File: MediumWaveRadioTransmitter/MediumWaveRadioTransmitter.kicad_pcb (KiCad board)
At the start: 2 copper layers, 16 parts, among them J1 Screw_Terminal_01x05, P6 100R, T3 BC337, T4 BC337, Y1 400 kH

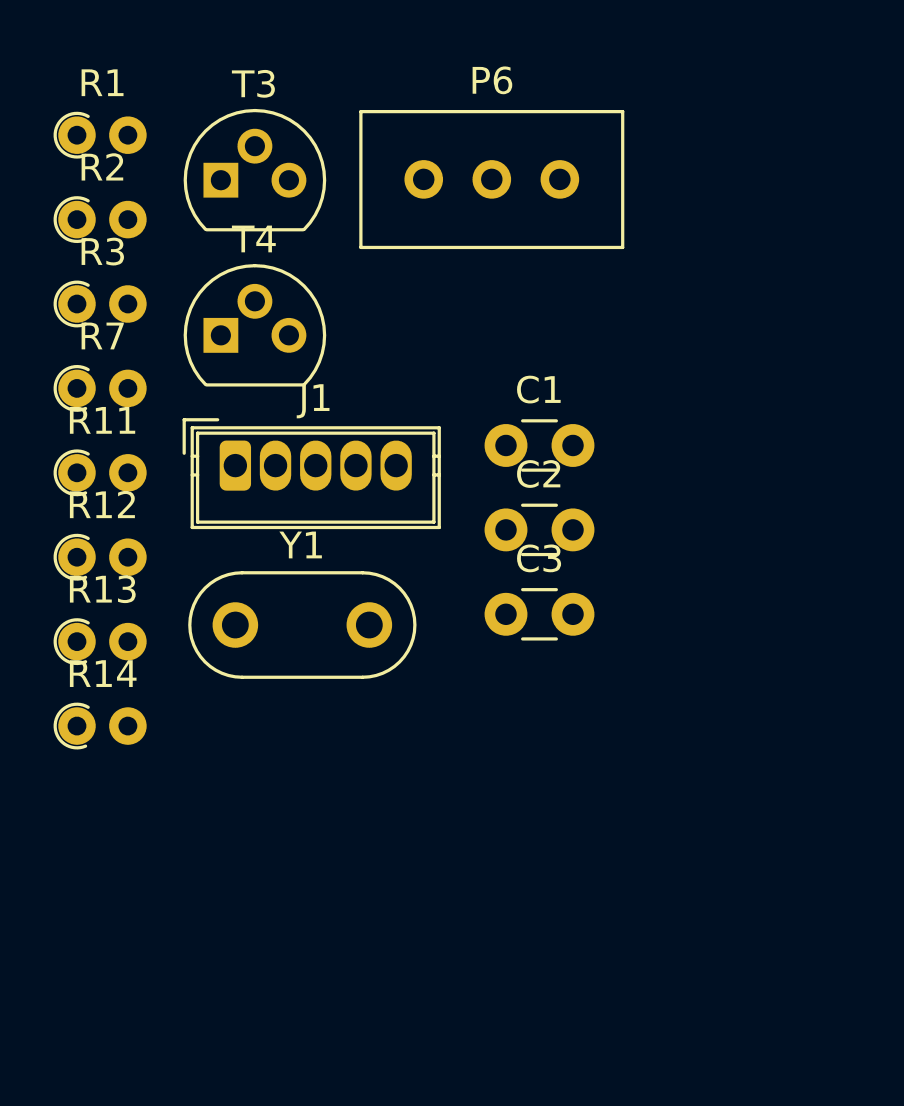
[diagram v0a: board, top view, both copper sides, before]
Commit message: feat: circuit diagram improved
changes:
- circuit diagram improved
- pcb layout routed

closes #1
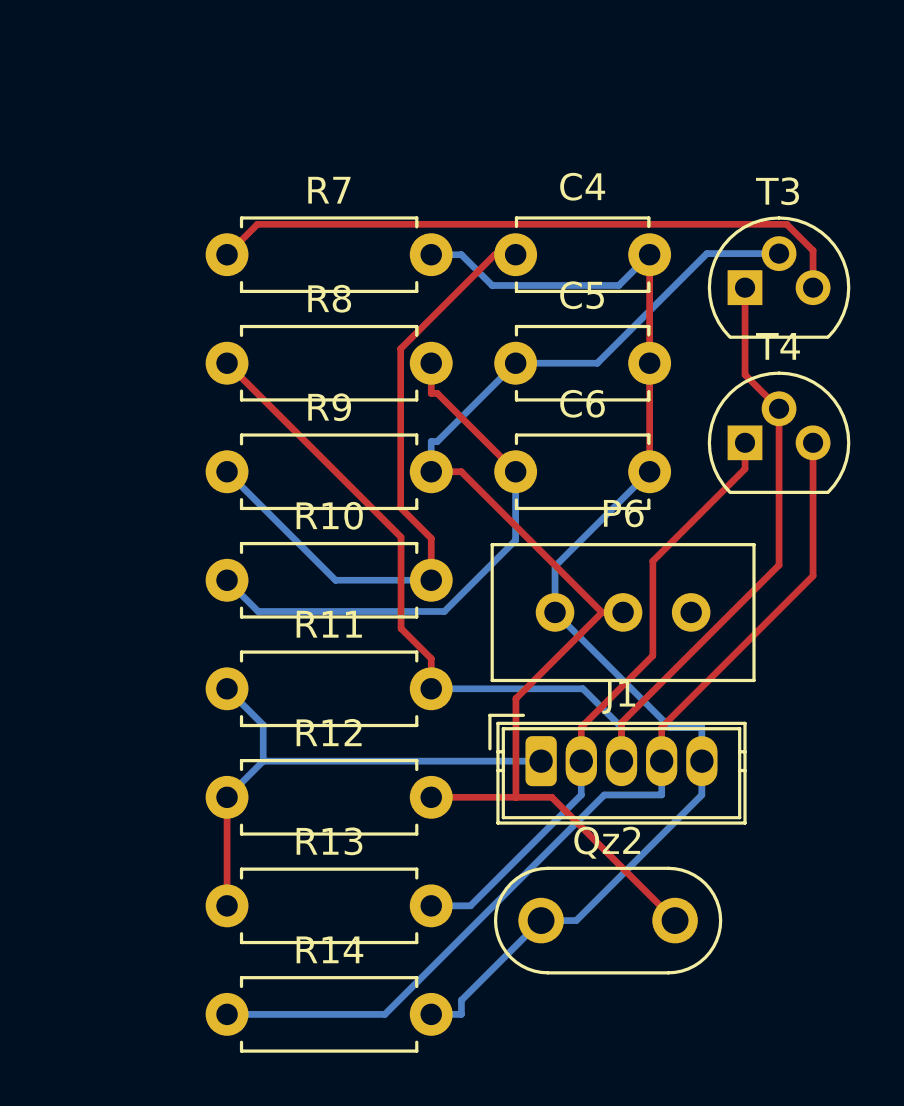
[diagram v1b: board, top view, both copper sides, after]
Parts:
- removed C1, C2, C3: C, Capacitor_THT:C_Disc_D3.0mm_W1.6mm_P2.50mm
- removed R1, R2, R3: 1k, Resistor_THT:R_Axial_DIN0204_L3.6mm_D1.6mm_P1.90mm_Vertical
- removed Y1: 400 kH, Crystal:Resonator-2Pin_W8.0mm_H3.5mm
- added C4: 1nF, Capacitor_THT:C_Disc_D4.7mm_W2.5mm_P5.00mm, F.Cu at (142.6, 83.1)
- added C5: 1nF, Capacitor_THT:C_Disc_D4.7mm_W2.5mm_P5.00mm, F.Cu at (142.6, 87.2)
- added C6: 1nF, Capacitor_THT:C_Disc_D4.7mm_W2.5mm_P5.00mm, F.Cu at (142.6, 91.2)
- added Qz2: 400kH, Crystal:Resonator-2Pin_W8.0mm_H3.5mm, F.Cu at (143.6, 108.0)
- added R10: 1k, Resistor_THT:R_Axial_DIN0207_L6.3mm_D2.5mm_P7.62mm_Horizontal, F.Cu at (131.9, 95.2)
- added R8: 1k, Resistor_THT:R_Axial_DIN0207_L6.3mm_D2.5mm_P7.62mm_Horizontal, F.Cu at (131.9, 87.2)
- added R9: 1k, Resistor_THT:R_Axial_DIN0207_L6.3mm_D2.5mm_P7.62mm_Horizontal, F.Cu at (131.9, 91.2)
- J1: value Screw_Terminal_01x05 -> WAGO 734-135
- R11, R12, R13, R14, R7: footprint Resistor_THT:R_Axial_DIN0204_L3.6mm_D1.6mm_P1.90mm_Vertical -> Resistor_THT:R_Axial_DIN0207_L6.3mm_D2.5mm_P7.62mm_Horizontal
- moved T3 20.0 mm to (151.2, 84.3)
- moved T4 20.0 mm to (151.2, 90.1)
- moved P6 16.9 mm to (149.2, 96.5)
- moved J1 15.9 mm to (143.6, 102.0)
- moved R14 12.1 mm to (131.9, 111.5)
- moved R13 11.3 mm to (131.9, 107.4)
- moved R12 10.6 mm to (131.9, 103.3)
- moved R11 9.81 mm to (131.9, 99.3)
- moved R7 7.50 mm to (131.9, 83.1)
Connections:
- P6 pad 3: Net-(J1-Pin_2) -> Net-(J1-Pin_5)
- R13 pad 2: Net-(J1-Pin_4) -> Net-(J1-Pin_2)
- R14 pad 1: Net-(J1-Pin_5) -> Net-(J1-Pin_4)
- R14 pad 2: Net-(J1-Pin_2) -> Net-(J1-Pin_5)
- R7 pad 2: Net-(J1-Pin_2) -> Net-(J1-Pin_5)
- T4 pad 1: Net-(J1-Pin_4) -> Net-(J1-Pin_2)
- T4 pad 3: Net-(J1-Pin_5) -> Net-(J1-Pin_4)
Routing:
- net Net-(J1-Pin_5): track 0.00 -> 47.5 mm
- net Net-(T3-B): track 0.00 -> 45.6 mm
- net Net-(J1-Pin_3): track 0.00 -> 44.9 mm
- net Net-(J1-Pin_4): track 0.00 -> 35.1 mm
- net Net-(C4-Pad1): track 0.00 -> 24.2 mm
- net Net-(T3-E): track 0.00 -> 24.1 mm
- net Net-(J1-Pin_2): track 0.00 -> 23.0 mm
- net Net-(C6-Pad1): track 0.00 -> 20.4 mm
- net Net-(J1-Pin_1): track 0.00 -> 19.6 mm
